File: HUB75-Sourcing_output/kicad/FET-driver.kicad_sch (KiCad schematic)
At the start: 7 parts, among them J12 Conn_01x02_Male, Q12 BSS84, U18 NSI45020AT1G

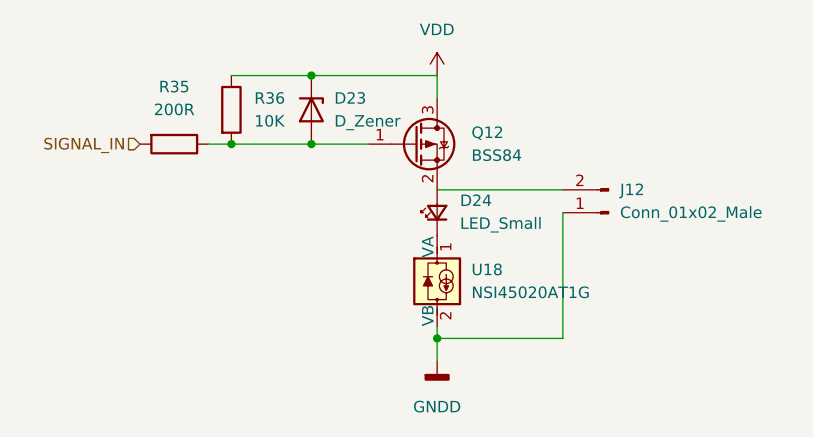
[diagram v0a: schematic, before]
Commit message: Update board with current mirror + backup
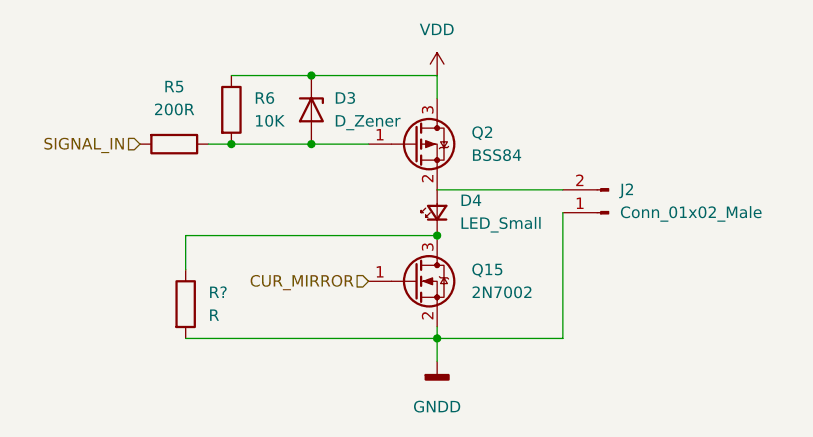
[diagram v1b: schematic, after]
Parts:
- removed U18: NSI45020AT1G, Diode_SMD:D_SOD-123, symbol Driver_LED:CL220K4-G
- added Q15: 2N7002, Package_TO_SOT_SMD:SOT-23, symbol Transistor_FET:2N7002
- added R?: R, symbol Device:R
- D4: renamed from D24; footprint LED_SMD:LED_2010_5025Metric_Pad1.52x2.65mm_HandSolder -> LED_SMD:LED_1206_3216Metric_Pad1.42x1.75mm_HandSolder
- R5: renamed from R35; footprint Resistor_SMD:R_2010_5025Metric_Pad1.40x2.65mm_HandSolder -> Resistor_SMD:R_1206_3216Metric_Pad1.30x1.75mm_HandSolder
- R6: renamed from R36; footprint Resistor_SMD:R_2010_5025Metric_Pad1.40x2.65mm_HandSolder -> Resistor_SMD:R_1206_3216Metric_Pad1.30x1.75mm_HandSolder
- renumbered D23 to D3, J12 to J2, Q12 to Q2
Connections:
- net GNDD: now also Q15.2 (S), R?.2
- net at D4.1 (K): now also Q15.3 (D), R?.1
- new net CUR_MIRROR: Q15.1 (G)
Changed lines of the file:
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@@
   (junction (at 72.39 35.56) (diameter 0) (color 0 0 0 0)
   )
+  (junction (at 86.36 45.72) (diameter 0) (color 0 0 0 0)
+  )
   (junction (at 72.39 27.94) (diameter 0) (color 0 0 0 0)
   )
@@
     (stroke (width 0) (type default) (color 0 0 0 0))
   )
+  (wire (pts (xy 58.42 57.15) (xy 86.36 57.15))
+    (stroke (width 0) (type default) (color 0 0 0 0))
+  )
   (wire (pts (xy 72.39 35.56) (xy 78.74 35.56))
     (stroke (width 0) (type default) (color 0 0 0 0))
   )
+  (wire (pts (xy 86.36 45.72) (xy 58.42 45.72))
+    (stroke (width 0) (type default) (color 0 0 0 0))
+  )
   (wire (pts (xy 100.33 57.15) (xy 86.36 57.15))
     (stroke (width 0) (type default) (color 0 0 0 0))
@@
     (stroke (width 0) (type default) (color 0 0 0 0))
   )
+  (wire (pts (xy 58.42 45.72) (xy 58.42 49.53))
+    (stroke (width 0) (type default) (color 0 0 0 0))
+  )
   (wire (pts (xy 63.5 35.56) (xy 72.39 35.56))
     (stroke (width 0) (type default) (color 0 0 0 0))
@@
   (wire (pts (xy 100.33 43.18) (xy 100.33 57.15))
     (stroke (width 0) (type default) (color 0 0 0 0))
+  )
+  (hierarchical_label "CUR_MIRROR" (shape input) (at 78.74 50.8 180)
+    (effects (font (size 1.27 1.27)) (justify right))
   )
   (hierarchical_label "SIGNAL_IN" (shape input) (at 53.34 35.56 180)
@@
   (symbol (lib_id "Device:LED_Small") (at 86.36 43.18 90)
     (in_bom yes) (on_board yes) (fields_autoplaced)
-    (property "Reference" "D24" (id 0) (at 88.9 41.8464 90)
+    (property "Reference" "D4" (id 0) (at 88.9 41.8464 90)
       (effects (font (size 1.27 1.27)) (justify right))
     )
@@
       (effects (font (size 1.27 1.27)) (justify right))
     )
-    (property "Footprint" "LED_SMD:LED_2010_5025Metric_Pad1.52x2.65mm_HandSolder" (id 2) (at 86.36 43.18 90)
+    (property "Footprint" "LED_SMD:LED_1206_3216Metric_Pad1.42x1.75mm_HandSolder" (id 2) (at 86.36 43.18 90)
       (effects (font (size 1.27 1.27)) hide)
     )
@@
   (symbol (lib_id "power:VDD") (at 86.36 27.94 0)
     (in_bom yes) (on_board yes) (fields_autoplaced)
-    (property "Reference" "#PWR041" (id 0) (at 86.36 31.75 0)
+    (property "Reference" "#PWR06" (id 0) (at 86.36 31.75 0)
       (effects (font (size 1.27 1.27)) hide)
     )
@@
   (symbol (lib_id "Transistor_FET:BSS84") (at 83.82 35.56 0)
     (in_bom yes) (on_board yes) (fields_autoplaced)
-    (property "Reference" "Q12" (id 0) (at 90.17 34.2899 0)
+    (property "Reference" "Q2" (id 0) (at 90.17 34.2899 0)
       (effects (font (size 1.27 1.27)) (justify left))
     )
@@
     (pin "3")
   )
+  (symbol (lib_id "Transistor_FET:2N7002") (at 83.82 50.8 0)
+    (in_bom yes) (on_board yes) (fields_autoplaced)
+    (property "Reference" "Q15" (id 0) (at 90.17 49.5299 0)
+      (effects (font (size 1.27 1.27)) (justify left))
+    )
+    (property "Value" "2N7002" (id 1) (at 90.17 52.0699 0)
+      (effects (font (size 1.27 1.27)) (justify left))
+    )
+    (property "Footprint" "Package_TO_SOT_SMD:SOT-23" (id 2) (at 88.9 52.705 0)
+      (effects (font (size 1.27 1.27) italic) (justify left) hide)
+    )
+    (property "Datasheet" "https://www.onsemi.com/pub/Collateral/NDS7002A-D.PDF" (id 3) (at 83.82 50.8 0)
+      (effects (font (size 1.27 1.27)) (justify left) hide)
+    )
+    (pin "1")
+    (pin "2")
+    (pin "3")
+  )
   (symbol (lib_id "Device:D_Zener") (at 72.39 31.75 270)
     (in_bom yes) (on_board yes) (fields_autoplaced)
-    (property "Reference" "D23" (id 0) (at 74.93 30.4799 90)
+    (property "Reference" "D3" (id 0) (at 74.93 30.4799 90)
       (effects (font (size 1.27 1.27)) (justify left))
     )
@@
   (symbol (lib_id "Connector:Conn_01x02_Male") (at 105.41 43.18 180)
     (in_bom yes) (on_board yes) (fields_autoplaced)
-    (property "Reference" "J12" (id 0) (at 106.68 40.6399 0)
+    (property "Reference" "J2" (id 0) (at 106.68 40.6399 0)
       (effects (font (size 1.27 1.27)) (justify right))
     )
@@
   (symbol (lib_id "power:GNDD") (at 86.36 59.69 0)
     (in_bom yes) (on_board yes) (fields_autoplaced)
-    (property "Reference" "#PWR042" (id 0) (at 86.36 66.04 0)
+    (property "Reference" "#PWR07" (id 0) (at 86.36 66.04 0)
       (effects (font (size 1.27 1.27)) hide)
     )
@@
     (pin "1")
   )
+  (symbol (lib_id "Device:R") (at 58.42 53.34 0)
+    (in_bom yes) (on_board yes) (fields_autoplaced)
+    (property "Reference" "R?" (id 0) (at 60.96 52.0699 0)
+      (effects (font (size 1.27 1.27)) (justify left))
+    )
+    (property "Value" "R" (id 1) (at 60.96 54.6099 0)
+      (effects (font (size 1.27 1.27)) (justify left))
+    )
+    (property "Footprint" "" (id 2) (at 56.642 53.34 90)
+      (effects (font (size 1.27 1.27)) hide)
+    )
+    (property "Datasheet" "~" (id 3) (at 58.42 53.34 0)
+      (effects (font (size 1.27 1.27)) hide)
+    )
+    (pin "1")
+    (pin "2")
+  )
   (symbol (lib_id "Device:R") (at 63.5 31.75 0)
     (in_bom yes) (on_board yes) (fields_autoplaced)
-    (property "Reference" "R36" (id 0) (at 66.04 30.4799 0)
+    (property "Reference" "R6" (id 0) (at 66.04 30.4799 0)
       (effects (font (size 1.27 1.27)) (justify left))
     )
@@
       (effects (font (size 1.27 1.27)) (justify left))
     )
-    (property "Footprint" "Resistor_SMD:R_2010_5025Metric_Pad1.40x2.65mm_HandSolder" (id 2) (at 61.722 31.75 90)
+    (property "Footprint" "Resistor_SMD:R_1206_3216Metric_Pad1.30x1.75mm_HandSolder" (id 2) (at 61.722 31.75 90)
       (effects (font (size 1.27 1.27)) hide)
     )
@@
   (symbol (lib_id "Device:R") (at 57.15 35.56 270)
     (in_bom yes) (on_board yes) (fields_autoplaced)
-    (property "Reference" "R35" (id 0) (at 57.15 29.21 90))
+    (property "Reference" "R5" (id 0) (at 57.15 29.21 90))
     (property "Value" "200R" (id 1) (at 57.15 31.75 90))
-    (property "Footprint" "Resistor_SMD:R_2010_5025Metric_Pad1.40x2.65mm_HandSolder" (id 2) (at 57.15 33.782 90)
+    (property "Footprint" "Resistor_SMD:R_1206_3216Metric_Pad1.30x1.75mm_HandSolder" (id 2) (at 57.15 33.782 90)
       (effects (font (size 1.27 1.27)) hide)
     )
@@
     (pin "2")
   )
-  (symbol (lib_id "Driver_LED:CL220K4-G") (at 86.36 50.8 0)
-    (in_bom yes) (on_board yes) (fields_autoplaced)
-    (property "Reference" "U18" (id 0) (at 90.17 49.5299 0)
-      (effects (font (size 1.27 1.27)) (justify left))
-    )
-    (property "Value" "NSI45020AT1G" (id 1) (at 90.17 52.0699 0)
-      (effects (font (size 1.27 1.27)) (justify left))
-    )
-    (property "Footprint" "Diode_SMD:D_SOD-123" (id 2) (at 90.17 52.07 0)
-      (effects (font (size 1.27 1.27)) (justify left) hide)
-    )
-    (property "Datasheet" "http://ww1.microchip.com/downloads/en/DeviceDoc/20005413A.pdf" (id 3) (at 86.614 50.8 0)
-      (effects (font (size 1.27 1.27)) hide)
-    )
-    (pin "1")
-    (pin "2")
-    (pin "3")
-  )
 )

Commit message: Update label
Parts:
- R38: renamed from R?; footprint (none) -> LED_SMD:LED_1206_3216Metric_Pad1.42x1.75mm_HandSolder
- renumbered D3 to D1, D4 to D2, J2 to J1, Q2 to Q1, Q15 to Q14, R5 to R3, R6 to R4
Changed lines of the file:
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@@
   (symbol (lib_id "Device:LED_Small") (at 86.36 43.18 90)
     (in_bom yes) (on_board yes) (fields_autoplaced)
-    (property "Reference" "D4" (id 0) (at 88.9 41.8464 90)
+    (property "Reference" "D2" (id 0) (at 88.9 41.8464 90)
       (effects (font (size 1.27 1.27)) (justify right))
     )
@@
   (symbol (lib_id "power:VDD") (at 86.36 27.94 0)
     (in_bom yes) (on_board yes) (fields_autoplaced)
-    (property "Reference" "#PWR06" (id 0) (at 86.36 31.75 0)
+    (property "Reference" "#PWR041" (id 0) (at 86.36 31.75 0)
       (effects (font (size 1.27 1.27)) hide)
     )
@@
   (symbol (lib_id "Transistor_FET:BSS84") (at 83.82 35.56 0)
     (in_bom yes) (on_board yes) (fields_autoplaced)
-    (property "Reference" "Q2" (id 0) (at 90.17 34.2899 0)
+    (property "Reference" "Q1" (id 0) (at 90.17 34.2899 0)
       (effects (font (size 1.27 1.27)) (justify left))
     )
@@
   (symbol (lib_id "Transistor_FET:2N7002") (at 83.82 50.8 0)
     (in_bom yes) (on_board yes) (fields_autoplaced)
-    (property "Reference" "Q15" (id 0) (at 90.17 49.5299 0)
+    (property "Reference" "Q14" (id 0) (at 90.17 49.5299 0)
       (effects (font (size 1.27 1.27)) (justify left))
     )
@@
   (symbol (lib_id "Device:D_Zener") (at 72.39 31.75 270)
     (in_bom yes) (on_board yes) (fields_autoplaced)
-    (property "Reference" "D3" (id 0) (at 74.93 30.4799 90)
+    (property "Reference" "D1" (id 0) (at 74.93 30.4799 90)
       (effects (font (size 1.27 1.27)) (justify left))
     )
@@
   (symbol (lib_id "Connector:Conn_01x02_Male") (at 105.41 43.18 180)
     (in_bom yes) (on_board yes) (fields_autoplaced)
-    (property "Reference" "J2" (id 0) (at 106.68 40.6399 0)
+    (property "Reference" "J1" (id 0) (at 106.68 40.6399 0)
       (effects (font (size 1.27 1.27)) (justify right))
     )
@@
   (symbol (lib_id "power:GNDD") (at 86.36 59.69 0)
     (in_bom yes) (on_board yes) (fields_autoplaced)
-    (property "Reference" "#PWR07" (id 0) (at 86.36 66.04 0)
+    (property "Reference" "#PWR042" (id 0) (at 86.36 66.04 0)
       (effects (font (size 1.27 1.27)) hide)
     )
@@
   (symbol (lib_id "Device:R") (at 58.42 53.34 0)
     (in_bom yes) (on_board yes) (fields_autoplaced)
-    (property "Reference" "R?" (id 0) (at 60.96 52.0699 0)
+    (property "Reference" "R38" (id 0) (at 60.96 52.0699 0)
       (effects (font (size 1.27 1.27)) (justify left))
     )
@@
       (effects (font (size 1.27 1.27)) (justify left))
     )
-    (property "Footprint" "" (id 2) (at 56.642 53.34 90)
+    (property "Footprint" "LED_SMD:LED_1206_3216Metric_Pad1.42x1.75mm_HandSolder" (id 2) (at 56.642 53.34 90)
       (effects (font (size 1.27 1.27)) hide)
     )
@@
   (symbol (lib_id "Device:R") (at 63.5 31.75 0)
     (in_bom yes) (on_board yes) (fields_autoplaced)
-    (property "Reference" "R6" (id 0) (at 66.04 30.4799 0)
+    (property "Reference" "R4" (id 0) (at 66.04 30.4799 0)
       (effects (font (size 1.27 1.27)) (justify left))
     )
@@
   (symbol (lib_id "Device:R") (at 57.15 35.56 270)
     (in_bom yes) (on_board yes) (fields_autoplaced)
-    (property "Reference" "R5" (id 0) (at 57.15 29.21 90))
+    (property "Reference" "R3" (id 0) (at 57.15 29.21 90))
     (property "Value" "200R" (id 1) (at 57.15 31.75 90))
     (property "Footprint" "Resistor_SMD:R_1206_3216Metric_Pad1.30x1.75mm_HandSolder" (id 2) (at 57.15 33.782 90)

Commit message: Remove incorrect GND connection
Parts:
- R38: now left out of the parts list
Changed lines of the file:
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@@
   (symbol (lib_id "power:VDD") (at 86.36 27.94 0)
     (in_bom yes) (on_board yes) (fields_autoplaced)
-    (property "Reference" "#PWR041" (id 0) (at 86.36 31.75 0)
+    (property "Reference" "#PWR04" (id 0) (at 86.36 31.75 0)
       (effects (font (size 1.27 1.27)) hide)
     )
@@
   (symbol (lib_id "power:GNDD") (at 86.36 59.69 0)
     (in_bom yes) (on_board yes) (fields_autoplaced)
-    (property "Reference" "#PWR042" (id 0) (at 86.36 66.04 0)
+    (property "Reference" "#PWR05" (id 0) (at 86.36 66.04 0)
       (effects (font (size 1.27 1.27)) hide)
     )
@@
   )
   (symbol (lib_id "Device:R") (at 58.42 53.34 0)
-    (in_bom yes) (on_board yes) (fields_autoplaced)
+    (in_bom no) (on_board yes) (fields_autoplaced)
     (property "Reference" "R38" (id 0) (at 60.96 52.0699 0)
       (effects (font (size 1.27 1.27)) (justify left))

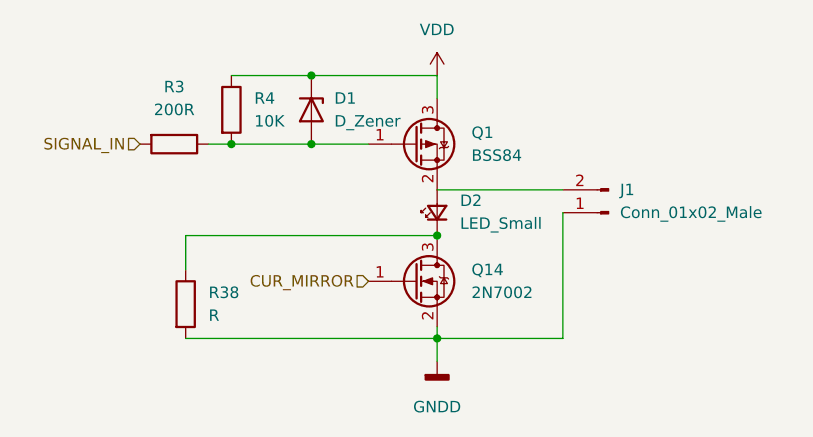
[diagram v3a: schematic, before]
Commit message: New version after prototype failed
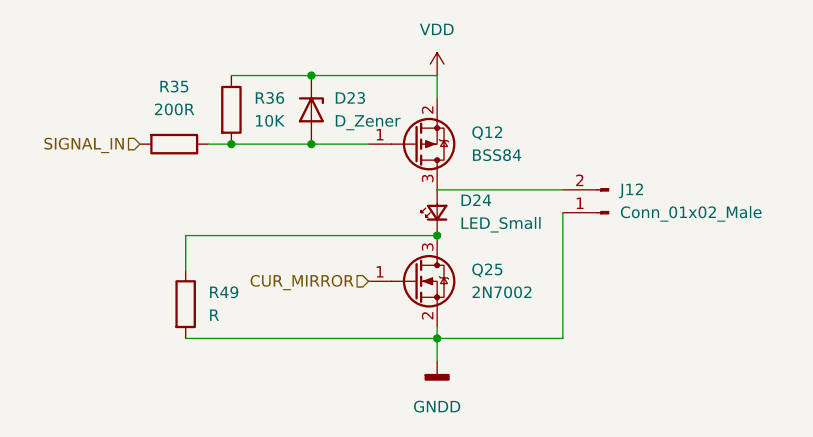
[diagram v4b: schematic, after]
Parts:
- renumbered D1 to D23, D2 to D24, J1 to J12, Q1 to Q12, Q14 to Q25, R3 to R35, R4 to R36, R38 to R49
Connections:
- net VDD: now also Q12.2 (S); no longer Q12.3 (D)
- net at D24.2 (A), J12.2 (Pin_2): now also Q12.3 (D); no longer Q12.2 (S)
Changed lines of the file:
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@@
   (symbol (lib_id "Device:LED_Small") (at 86.36 43.18 90)
     (in_bom yes) (on_board yes) (fields_autoplaced)
-    (property "Reference" "D2" (id 0) (at 88.9 41.8464 90)
+    (property "Reference" "D24" (id 0) (at 88.9 41.8464 90)
       (effects (font (size 1.27 1.27)) (justify right))
     )
@@
   (symbol (lib_id "power:VDD") (at 86.36 27.94 0)
     (in_bom yes) (on_board yes) (fields_autoplaced)
-    (property "Reference" "#PWR04" (id 0) (at 86.36 31.75 0)
+    (property "Reference" "#PWR041" (id 0) (at 86.36 31.75 0)
       (effects (font (size 1.27 1.27)) hide)
     )
@@
     (pin "1")
   )
-  (symbol (lib_id "Transistor_FET:BSS84") (at 83.82 35.56 0)
+  (symbol (lib_id "Transistor_FET:BSS84") (at 83.82 35.56 0) (mirror x)
     (in_bom yes) (on_board yes) (fields_autoplaced)
-    (property "Reference" "Q1" (id 0) (at 90.17 34.2899 0)
+    (property "Reference" "Q12" (id 0) (at 90.17 34.2899 0)
       (effects (font (size 1.27 1.27)) (justify left))
     )
@@
       (effects (font (size 1.27 1.27)) (justify left))
     )
-    (property "Footprint" "Package_TO_SOT_SMD:SOT-23" (id 2) (at 88.9 37.465 0)
+    (property "Footprint" "Package_TO_SOT_SMD:SOT-23" (id 2) (at 88.9 33.655 0)
       (effects (font (size 1.27 1.27) italic) (justify left) hide)
     )
@@
   (symbol (lib_id "Transistor_FET:2N7002") (at 83.82 50.8 0)
     (in_bom yes) (on_board yes) (fields_autoplaced)
-    (property "Reference" "Q14" (id 0) (at 90.17 49.5299 0)
+    (property "Reference" "Q25" (id 0) (at 90.17 49.5299 0)
       (effects (font (size 1.27 1.27)) (justify left))
     )
@@
   (symbol (lib_id "Device:D_Zener") (at 72.39 31.75 270)
     (in_bom yes) (on_board yes) (fields_autoplaced)
-    (property "Reference" "D1" (id 0) (at 74.93 30.4799 90)
+    (property "Reference" "D23" (id 0) (at 74.93 30.4799 90)
       (effects (font (size 1.27 1.27)) (justify left))
     )
@@
   (symbol (lib_id "Connector:Conn_01x02_Male") (at 105.41 43.18 180)
     (in_bom yes) (on_board yes) (fields_autoplaced)
-    (property "Reference" "J1" (id 0) (at 106.68 40.6399 0)
+    (property "Reference" "J12" (id 0) (at 106.68 40.6399 0)
       (effects (font (size 1.27 1.27)) (justify right))
     )
@@
   (symbol (lib_id "power:GNDD") (at 86.36 59.69 0)
     (in_bom yes) (on_board yes) (fields_autoplaced)
-    (property "Reference" "#PWR05" (id 0) (at 86.36 66.04 0)
+    (property "Reference" "#PWR042" (id 0) (at 86.36 66.04 0)
       (effects (font (size 1.27 1.27)) hide)
     )
@@
   (symbol (lib_id "Device:R") (at 58.42 53.34 0)
     (in_bom no) (on_board yes) (fields_autoplaced)
-    (property "Reference" "R38" (id 0) (at 60.96 52.0699 0)
+    (property "Reference" "R49" (id 0) (at 60.96 52.0699 0)
       (effects (font (size 1.27 1.27)) (justify left))
     )
@@
   (symbol (lib_id "Device:R") (at 63.5 31.75 0)
     (in_bom yes) (on_board yes) (fields_autoplaced)
-    (property "Reference" "R4" (id 0) (at 66.04 30.4799 0)
+    (property "Reference" "R36" (id 0) (at 66.04 30.4799 0)
       (effects (font (size 1.27 1.27)) (justify left))
     )
@@
   (symbol (lib_id "Device:R") (at 57.15 35.56 270)
     (in_bom yes) (on_board yes) (fields_autoplaced)
-    (property "Reference" "R3" (id 0) (at 57.15 29.21 90))
+    (property "Reference" "R35" (id 0) (at 57.15 29.21 90))
     (property "Value" "200R" (id 1) (at 57.15 31.75 90))
     (property "Footprint" "Resistor_SMD:R_1206_3216Metric_Pad1.30x1.75mm_HandSolder" (id 2) (at 57.15 33.782 90)
